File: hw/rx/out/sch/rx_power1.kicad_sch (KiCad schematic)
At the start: 16 parts, among them J1 backplane 2x13, U4 TLV76733, U5 TLV76733

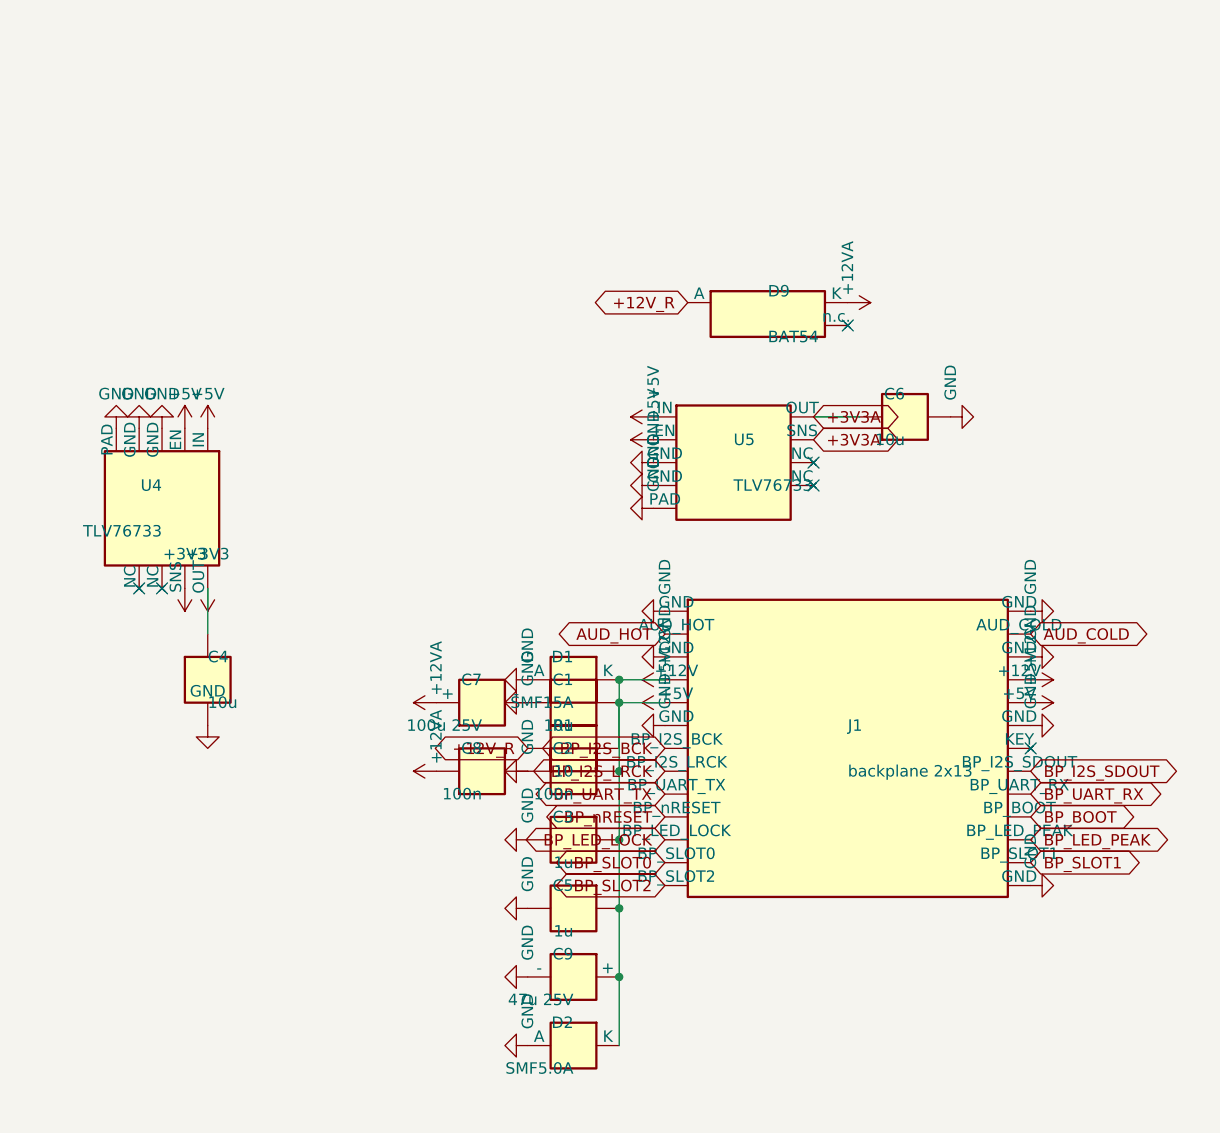
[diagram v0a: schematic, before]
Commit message: hw/rx + hw/pack: #116 review fixes: netclass pour clearances (no 0.09 mm override), keyed J1 with no hole at 14, solid RF grounds, K1 pin-1/CPL rotation, raw RF numbers (#34)
- M1: JLC copper-clearance rule removed from rx and pack .kicad_dru; boards refilled/regenerated; probe-rule tests
  assert >= 0.125 mm everywhere and >= 0.15 mm to Audio_I on the committed fill; outer-copper rule width-independent
- S1: openpack:PinHeader_2x13_P2.54mm_Key14 (pad 14 deleted, KEY silk), header XFCN PZ254V-12-26P (LCSC C22465887,
  pin 14 cut), main-board socket Samtec SSW-113-01-G-D-14 recorded in ADR-0014; test
- S2: zone_connect solid on J3-J5, U2, U1 GND pads; test
- S3: TQ2SA pin-1 dot + '+', CPL +270 for the relay (K1 at 180); pin-1 marker + CPL test for all polarized parts
- N1 raw RF Z0 (51.5 bare / ~49.3 masked), N3 C44 at U6, REVIEW follow-ups

Co-Authored-By: Claude Opus 5.5 <noreply@anthropic.com>
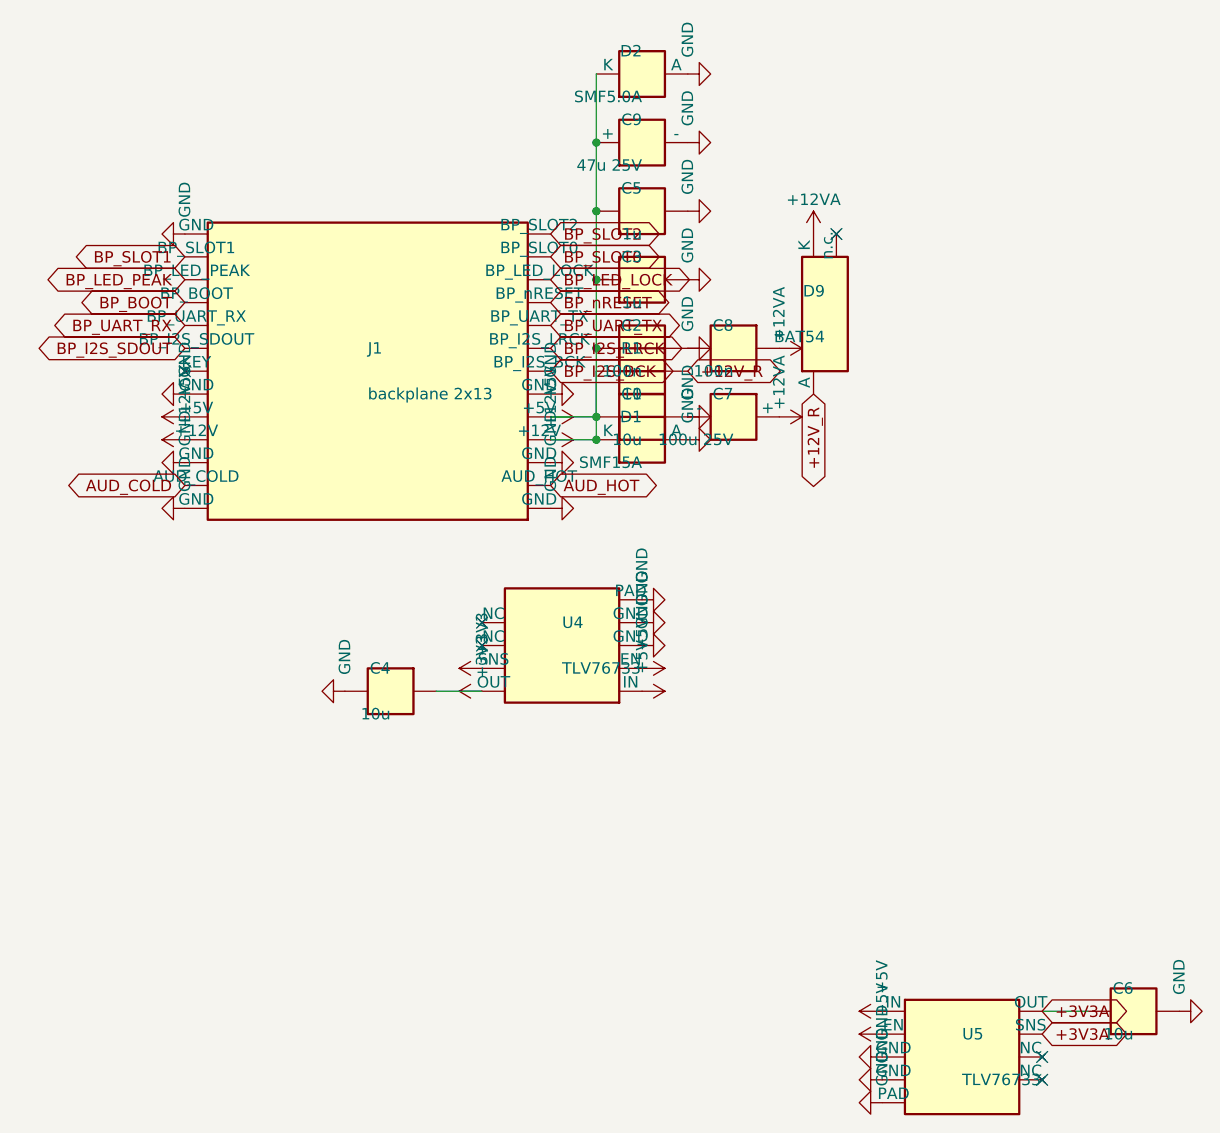
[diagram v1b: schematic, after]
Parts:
- J1: footprint Connector_PinHeader_2.54mm:PinHeader_2x13_P2.54mm_Vertical -> openpack:PinHeader_2x13_P2.54mm_Key14; MPN HDR_2x13_2.54_KEY14 -> PZ254V-12-26P
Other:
- moved on the sheet: C1, C2, C3, C4, C5, C6, C7, C8, C9, D1, D2, D9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
